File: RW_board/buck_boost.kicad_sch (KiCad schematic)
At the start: 43 parts, among them IC201 MAX44284WAUT+T, Q201 BSZ300N15NS5ATMA1, U201 LM5022MM

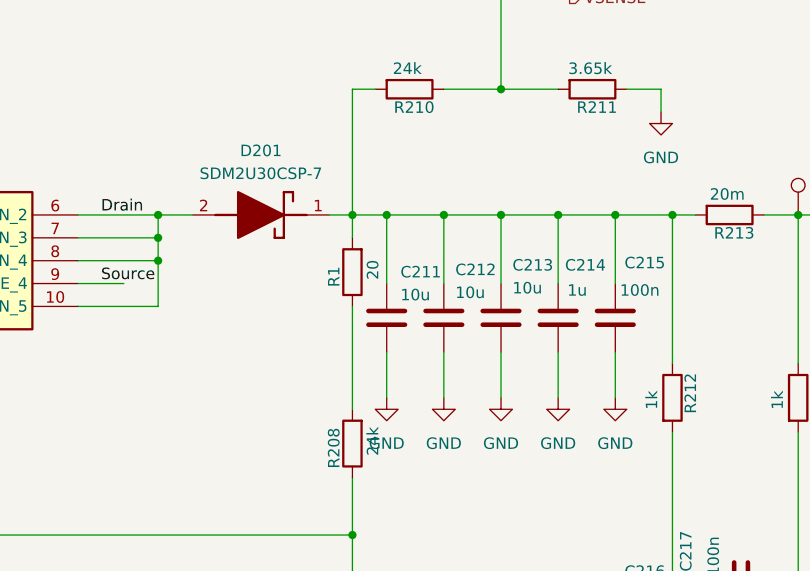
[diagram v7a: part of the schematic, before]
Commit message: Boost Testpoint Update
2 Testpoints added to schematic and layout
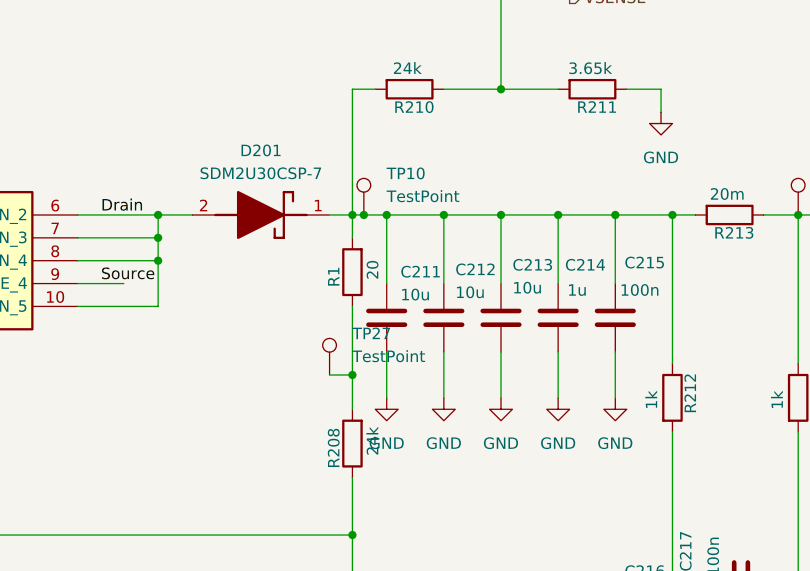
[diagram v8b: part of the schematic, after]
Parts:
- added TP10, TP27: TestPoint, TestPoint:TestPoint_Pad_1.0x1.0mm, symbol Connector:TestPoint
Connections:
- net at C211.1, C212.1, C213.1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: now also TP10.1
- net at R1.1, R208.2: now also TP27.1
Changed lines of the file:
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@@
 	)
 	(junction
+		(at 227.33 43.18)
+		(diameter 0)
+		(color 0 0 0 0)
+	)
+	(junction
 		(at 236.22 43.18)
 		(diameter 0)
@@
 	)
 	(junction
+		(at 226.06 60.96)
+		(diameter 0)
+		(color 0 0 0 0)
+	)
+	(junction
 		(at 146.05 45.72)
 		(diameter 0)
@@
 	(wire
 		(pts
+			(xy 227.33 43.18) (xy 229.87 43.18)
+		)
+		(stroke
+			(width 0)
+			(type default)
+		)
+	)
+	(wire
+		(pts
 			(xy 261.62 111.76) (xy 261.62 106.68)
 		)
@@
 	(wire
 		(pts
+			(xy 226.06 60.96) (xy 226.06 53.34)
+		)
+		(stroke
+			(width 0)
+			(type default)
+		)
+	)
+	(wire
+		(pts
 			(xy 261.62 67.31) (xy 261.62 83.82)
 		)
@@
 	(wire
 		(pts
+			(xy 223.52 60.96) (xy 226.06 60.96)
+		)
+		(stroke
+			(width 0)
+			(type default)
+		)
+	)
+	(wire
+		(pts
 			(xy 149.86 53.34) (xy 149.86 50.8)
 		)
@@
 	(wire
 		(pts
-			(xy 226.06 64.77) (xy 226.06 53.34)
+			(xy 226.06 64.77) (xy 226.06 60.96)
 		)
 		(stroke
@@
 	(wire
 		(pts
-			(xy 226.06 43.18) (xy 229.87 43.18)
+			(xy 226.06 43.18) (xy 227.33 43.18)
 		)
 		(stroke
@@
 	(label "Drain"
 		(at 153.67 53.34 0)
+		(fields_autoplaced yes)
 		(effects
 			(font
@@
 	(label "Source"
 		(at 198.12 50.8 0)
+		(fields_autoplaced yes)
 		(effects
 			(font
@@
 	(label "UVLO"
 		(at 68.58 71.12 0)
+		(fields_autoplaced yes)
 		(effects
 			(font
@@
 	(label "Sense-"
 		(at 236.22 100.33 0)
+		(fields_autoplaced yes)
 		(effects
 			(font
@@
 	(label "Drain"
 		(at 198.12 43.18 0)
+		(fields_autoplaced yes)
 		(effects
 			(font
@@
 	(label "Source"
 		(at 146.05 43.18 0)
+		(fields_autoplaced yes)
 		(effects
 			(font
@@
 	(label "Sense+"
 		(at 264.16 104.14 0)
+		(fields_autoplaced yes)
 		(effects
 			(font
@@
 	(label "Feedback"
 		(at 152.4 78.74 0)
+		(fields_autoplaced yes)
 		(effects
 			(font
@@
 		(shape input)
 		(at 274.32 109.22 0)
+		(fields_autoplaced yes)
 		(effects
 			(font
@@
 		(shape output)
 		(at 250.19 19.05 0)
+		(fields_autoplaced yes)
 		(effects
 			(font
@@
 		(shape output)
 		(at 223.52 106.68 180)
+		(fields_autoplaced yes)
 		(effects
 			(font
@@
 		(shape input)
 		(at 22.86 50.8 180)
+		(fields_autoplaced yes)
 		(effects
 			(font
@@
 		(shape output)
 		(at 278.13 43.18 0)
+		(fields_autoplaced yes)
 		(effects
 			(font
@@
 	)
 	(symbol
+		(lib_id "Connector:TestPoint")
+		(at 227.33 43.18 0)
+		(unit 1)
+		(exclude_from_sim no)
+		(in_bom yes)
+		(on_board yes)
+		(dnp no)
+		(fields_autoplaced yes)
+		(property "Reference" "TP10"
+			(at 229.87 38.6079 0)
+			(effects
+				(font
+					(size 1.27 1.27)
+				)
+				(justify left)
+			)
+		)
+		(property "Value" "TestPoint"
+			(at 229.87 41.1479 0)
+			(effects
+				(font
+					(size 1.27 1.27)
+				)
+				(justify left)
+			)
+		)
+		(property "Footprint" "TestPoint:TestPoint_Pad_1.0x1.0mm"
+			(at 232.41 43.18 0)
+			(effects
+				(font
+					(size 1.27 1.27)
+				)
+				(hide yes)
+			)
+		)
+		(property "Datasheet" "~"
+			(at 232.41 43.18 0)
+			(effects
+				(font
+					(size 1.27 1.27)
+				)
+				(hide yes)
+			)
+		)
+		(property "Description" "test point"
+			(at 227.33 43.18 0)
+			(effects
+				(font
+					(size 1.27 1.27)
+				)
+				(hide yes)
+			)
+		)
+		(pin "1"
+		)
+		(instances
+			(project "RW_board"
+				(path "/ff273890-9ca6-499d-9c73-a93557b69e48/818fd1d9-2c7b-4967-b4fa-637005b787d9"
+					(reference "TP10")
+					(unit 1)
+				)
+			)
+		)
+	)
+	(symbol
 		(lib_id "Device:C")
 		(at 266.7 114.3 180)
@@
 					(unit 1)
 				)
+			)
+		)
+	)
+	(symbol
+		(lib_id "Connector:TestPoint")
+		(at 223.52 60.96 0)
+		(unit 1)
+		(exclude_from_sim no)
+		(in_bom yes)
+		(on_board yes)
+		(dnp no)
+		(fields_autoplaced yes)
+		(property "Reference" "TP27"
+			(at 226.06 56.3879 0)
+			(effects
+				(font
+					(size 1.27 1.27)
+				)
+				(justify left)
+			)
+		)
+		(property "Value" "TestPoint"
+			(at 226.06 58.9279 0)
+			(effects
+				(font
+					(size 1.27 1.27)
+				)
+				(justify left)
+			)
+		)
+		(property "Footprint" "TestPoint:TestPoint_Pad_1.0x1.0mm"
+			(at 228.6 60.96 0)
+			(effects
+				(font
+					(size 1.27 1.27)
+				)
+				(hide yes)
+			)
+		)
+		(property "Datasheet" "~"
+			(at 228.6 60.96 0)
+			(effects
+				(font
+					(size 1.27 1.27)
+				)
+				(hide yes)
+			)
+		)
+		(property "Description" "test point"
+			(at 223.52 60.96 0)
+			(effects
+				(font
+					(size 1.27 1.27)
+				)
+				(hide yes)
+			)
+		)
+		(pin "1"
+		)
+		(instances
+			(project "RW_board"
+				(path "/ff273890-9ca6-499d-9c73-a93557b69e48/818fd1d9-2c7b-4967-b4fa-637005b787d9"
+					(reference "TP27")
+					(unit 1)
+				)
